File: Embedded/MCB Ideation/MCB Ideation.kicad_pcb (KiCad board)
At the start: 2 copper layers, 19.2 x 26.6 mm, 22 parts, among them J2 USB, J3 MicroSD, U1 ICM-20948, U2 BME280, U4 AP7366-33W5-7

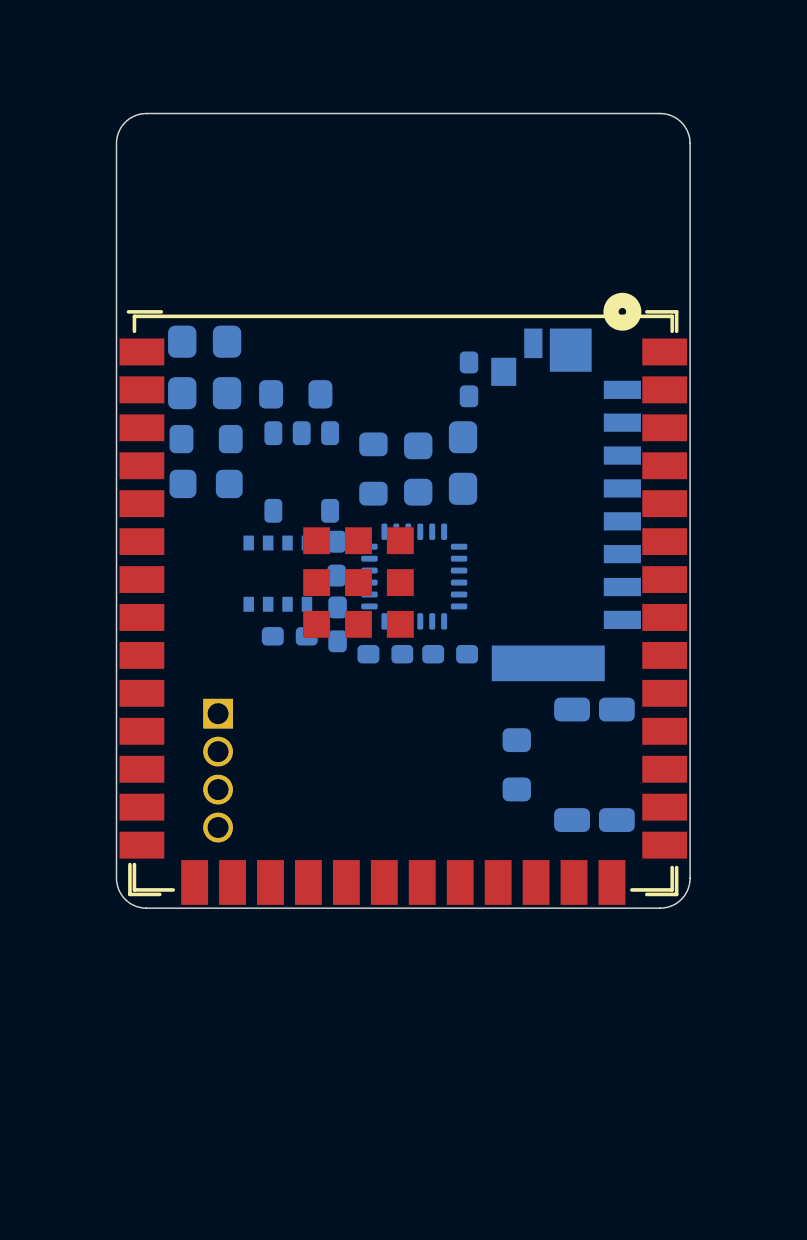
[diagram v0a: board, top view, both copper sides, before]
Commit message: Added Sensored
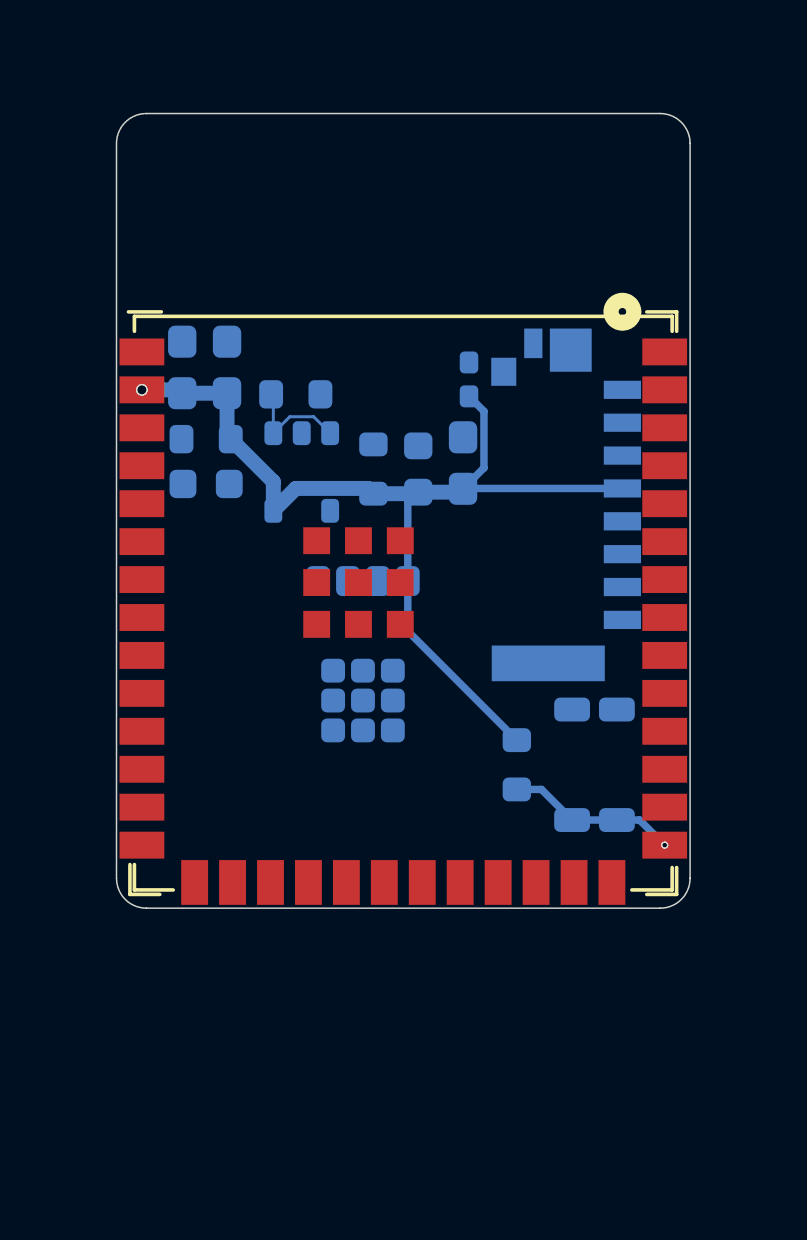
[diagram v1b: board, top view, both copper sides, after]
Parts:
- removed C1, C2, C3: 0.1uF, Capacitor_SMD:C_0402_1005Metric_Pad0.74x0.62mm_HandSolder
- removed C4, C5: 100nF, Capacitor_SMD:C_0402_1005Metric_Pad0.74x0.62mm_HandSolder
- removed J2: USB, Connector_PinSocket_1.27mm:PinSocket_1x04_P1.27mm_Vertical
- removed U2: BME280, Package_LGA:Bosch_LGA-8_2.5x2.5mm_P0.65mm_ClockwisePinNumbering
- U1: value ICM-20948 -> Sensored; footprint Sensor_Motion:InvenSense_QFN-24_3x3mm_P0.4mm -> Sensored:Sensored
- moved U1 4.49 mm to (138.7, 103.0), turned to 90 degrees
- turned C9 to 90 degrees
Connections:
- net /Vin renamed Net-(U4-EN)
- C12 pad 1: /3V3 -> +3V3
- C13 pad 1: /3V3 -> +3V3
- U1 pad 1: unconnected-(U1-NC-Pad1) -> +3V3
- U1 pad 2: unconnected-(U1-NC-Pad2) -> Sensor SDA
- U1 pad 3: unconnected-(U1-NC-Pad3) -> Sensor SCL
- U1 pad 4: unconnected-(U1-NC-Pad4) -> GND
- U4 pad 5: /3V3 -> +3V3
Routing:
- net +3V3: track 0.00 -> 33.2 mm, vias 0 -> 1
- net Net-(ESP1-GPIO0/BOOT): track 0.00 -> 5.72 mm, vias 0 -> 1
- net Net-(U4-EN): track 0.00 -> 3.69 mm

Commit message: Added Expansion Pins
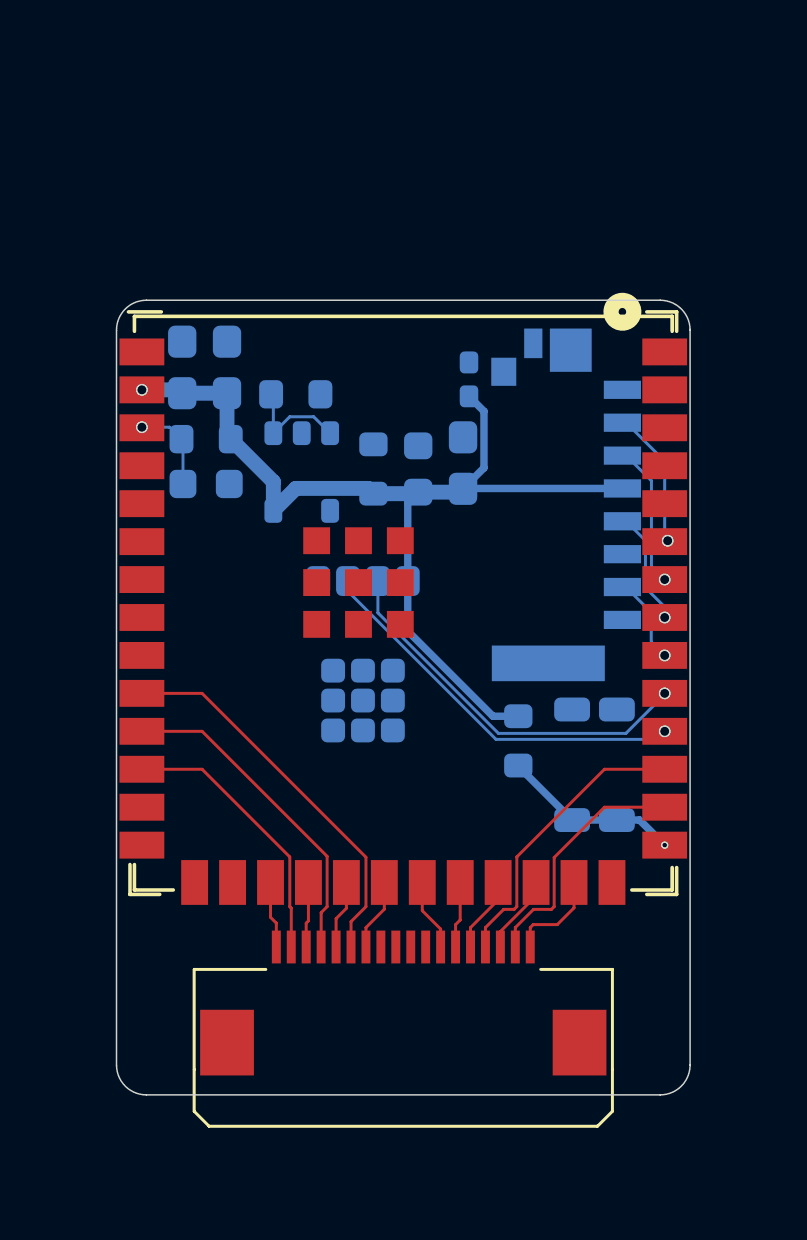
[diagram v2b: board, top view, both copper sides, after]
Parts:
- added U2: ~, FFC_Connector:FFC Aliexpress 0.5mm 18P, F.Cu at (140.0, 112.2)
- moved R2 0.80 mm to (143.8, 104.3)
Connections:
- ESP1 pad 10: unconnected-(ESP1-GPIO17/U1TXD/ADC2_CH6-Pad10) -> Exp 5
- ESP1 pad 11: unconnected-(ESP1-GPIO18/U1RXD/ADC2_CH7/CLK_OUT3-Pad11) -> Exp 3
- ESP1 pad 12: unconnected-(ESP1-GPIO8/TOUCH8/ADC1_CH7/SUBSPICS1-Pad12) -> Exp 1
- ESP1 pad 17: unconnected-(ESP1-GPIO9/TOUCH9/ADC1_CH8/FSPIHD/SUBSPIHD-Pad17) -> Exp 0
- ESP1 pad 18: unconnected-(ESP1-GPIO10/TOUCH10/ADC1_CH9/FSPICS0/FSPIIO4/SUBSPICS0-Pad18) -> Exp 2
- ESP1 pad 19: unconnected-(ESP1-GPIO11/TOUCH11/ADC2_CH0/FSPID/FSPIIO5/SUBSPID-Pad19) -> Exp 4
- ESP1 pad 20: unconnected-(ESP1-GPIO12/TOUCH12/ADC2_CH1/FSPICLK/FSPIIO6/SUBSPICLK-Pad20) -> Exp 6
- ESP1 pad 21: unconnected-(ESP1-GPIO13/TOUCH13/ADC2_CH2/FSPIQ/FSPIIO7/SUBSPIQ-Pad21) -> Exp 7
- ESP1 pad 22: unconnected-(ESP1-GPIO14/TOUCH14/ADC2_CH3/FSPIWP/FSPIDQS/SUBSPIWP-Pad22) -> Exp 8
- ESP1 pad 23: unconnected-(ESP1-GPIO21-Pad23) -> Exp 9
- ESP1 pad 24: unconnected-(ESP1-GPIO47/SPICLK_P/SUBSPICLK_P_DIFF-Pad24) -> Exp 11
- ESP1 pad 25: unconnected-(ESP1-GPIO48/SPICLK_N/SUBSPICLK_N_DIFF-Pad25) -> Exp 13
- ESP1 pad 28: unconnected-(ESP1-SPIIO6/GPIO35/FSPID/SUBSPID-Pad28) -> Exp 12
- ESP1 pad 29: unconnected-(ESP1-SPIIO7/GPIO36/FSPICLK/SUBSPICLK-Pad29) -> Exp 10
- ESP1 pad 30: unconnected-(ESP1-SPIDQS/GPIO37/FSPIQ/SUBSPIQ-Pad30) -> Sensor SCL
- ESP1 pad 31: unconnected-(ESP1-GPIO38/FSPIWP/SUBSPIWP-Pad31) -> Sensor SDA
- ESP1 pad 32: unconnected-(ESP1-MTCK/GPIO39/CLK_OUT3/SUBSPICS1-Pad32) -> SD SPI MISO
- ESP1 pad 33: unconnected-(ESP1-MTDO/GPIO40/CLK_OUT2-Pad33) -> SD SPI CLK
- ESP1 pad 34: unconnected-(ESP1-MTDI/GPIO41/CLK_OUT1-Pad34) -> SD SPI MOSI
- ESP1 pad 35: unconnected-(ESP1-MTMS/GPIO42-Pad35) -> SD SPI CS
- J3 pad 2: unconnected-(J3-Pad2) -> SD SPI CS
- J3 pad 3: unconnected-(J3-Pad3) -> SD SPI MOSI
- J3 pad 5: unconnected-(J3-Pad5) -> SD SPI CLK
- J3 pad 6: unconnected-(J3-Pad6) -> GND
- J3 pad 7: unconnected-(J3-Pad7) -> SD SPI MISO
- J3 pad G1: unconnected-(J3-PadG1) -> GND
- J3 pad G2: unconnected-(J3-PadG2) -> GND
- J3 pad G3: unconnected-(J3-PadG3) -> GND
- J3 pad G4: unconnected-(J3-PadG4) -> GND
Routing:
- net Sensor SCL: track 0.00 -> 13.1 mm, vias 0 -> 1
- net Exp 5: track 0.00 -> 13.0 mm
- net Sensor SDA: track 0.00 -> 12.9 mm, vias 0 -> 1
- net Exp 3: track 0.00 -> 11.1 mm
- net Exp 10: track 0.00 -> 9.82 mm
- net Exp 1: track 0.00 -> 9.20 mm
- net Exp 12: track 0.00 -> 8.28 mm
- net SD SPI CS: track 0.00 -> 5.04 mm, vias 0 -> 1
- net SD SPI MOSI: track 0.00 -> 4.81 mm, vias 0 -> 1
- net SD SPI CLK: track 0.00 -> 3.88 mm, vias 0 -> 1
- net Exp 13: track 0.00 -> 3.24 mm
- net Net-(ESP1-EN): track 0.00 -> 3.03 mm, vias 0 -> 1
- net SD SPI MISO: track 0.00 -> 2.94 mm, vias 0 -> 1
- net Exp 11: track 0.00 -> 2.65 mm
- net Exp 9: track 0.00 -> 2.54 mm
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
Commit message: Added USB Connectivity & Verified Expansion Pins
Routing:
- net USB -: track 0.00 -> 14.9 mm, vias 0 -> 2
- net USB +: track 0.00 -> 12.2 mm
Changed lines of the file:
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@@
 		(net 5)
+	)
+	(segment
+		(start 131.1 109.422206)
+		(end 134.602794 112.925)
+		(width 0.2)
+		(layer "F.Cu")
+		(net 9)
+	)
+	(segment
+		(start 140.25 112.025001)
+		(end 140.25 111.2)
+		(width 0.2)
+		(layer "F.Cu")
+		(net 9)
+	)
+	(segment
+		(start 140.225 112.050001)
+		(end 140.25 112.025001)
+		(width 0.2)
+		(layer "F.Cu")
+		(net 9)
+	)
+	(segment
+		(start 140.225 112.2932)
+		(end 140.225 112.050001)
+		(width 0.2)
+		(layer "F.Cu")
+		(net 9)
+	)
+	(segment
+		(start 139.5932 112.925)
+		(end 140.225 112.2932)
+		(width 0.2)
+		(layer "F.Cu")
+		(net 9)
+	)
+	(segment
+		(start 134.602794 112.925)
+		(end 139.5932 112.925)
+		(width 0.2)
+		(layer "F.Cu")
+		(net 9)
+	)
+	(segment
+		(start 131.1 108.75)
+		(end 131.1 109.422206)
+		(width 0.2)
+		(layer "F.Cu")
+		(net 9)
+	)
+	(via
+		(at 131.1 108.75)
+		(size 0.4)
+		(drill 0.3)
+		(layers "F.Cu" "B.Cu")
+		(net 9)
+	)
+	(via
+		(at 131.25 106.52)
+		(size 0.4)
+		(drill 0.3)
+		(layers "F.Cu" "B.Cu")
+		(net 9)
+	)
+	(segment
+		(start 131.25 108.6)
+		(end 131.1 108.75)
+		(width 0.2)
+		(layer "B.Cu")
+		(net 9)
+	)
+	(segment
+		(start 131.25 106.52)
+		(end 131.25 108.6)
+		(width 0.2)
+		(layer "B.Cu")
+		(net 9)
+	)
+	(segment
+		(start 139.775 112.1068)
+		(end 139.775 112.050001)
+		(width 0.2)
+		(layer "F.Cu")
+		(net 10)
+	)
+	(segment
+		(start 131.6 108.14)
+		(end 131.6 109.25)
+		(width 0.2)
+		(layer "F.Cu")
+		(net 10)
+	)
+	(segment
+		(start 139.75 112.025001)
+		(end 139.75 111.2)
+		(width 0.2)
+		(layer "F.Cu")
+		(net 10)
+	)
+	(segment
+		(start 139.775 112.050001)
+		(end 139.75 112.025001)
+		(width 0.2)
+		(layer "F.Cu")
+		(net 10)
+	)
+	(segment
+		(start 131.25 107.79)
+		(end 131.6 108.14)
+		(width 0.2)
+		(layer "F.Cu")
+		(net 10)
+	)
+	(segment
+		(start 139.4068 112.475)
+		(end 139.775 112.1068)
+		(width 0.2)
+		(layer "F.Cu")
+		(net 10)
+	)
+	(segment
+		(start 131.6 109.25)
+		(end 134.825 112.475)
+		(width 0.2)
+		(layer "F.Cu")
+		(net 10)
+	)
+	(segment
+		(start 134.825 112.475)
+		(end 139.4068 112.475)
+		(width 0.2)
+		(layer "F.Cu")
+		(net 10)
 	)
 	(via

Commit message: Added Secondary Expansion (Comms Link)
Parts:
- added U3: ~, FFC_Connector:FFC Aliexpress 0.5mm 6P, B.Cu at (140.0, 112.2)
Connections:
- net Net-(U4-EN) renamed +5V
- ESP1 pad 8: unconnected-(ESP1-GPIO15/U0RTS/ADC2_CH4/XTAL_32K_P-Pad8) -> EXP UART TX
- ESP1 pad 9: unconnected-(ESP1-GPIO16/U0CTS/ADC2_CH5/XTAL_32K_N-Pad9) -> EXP UART RX
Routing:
- net EXP UART TX: track 0.00 -> 15.5 mm, vias 0 -> 1
- net EXP UART RX: track 0.00 -> 13.9 mm, vias 0 -> 1

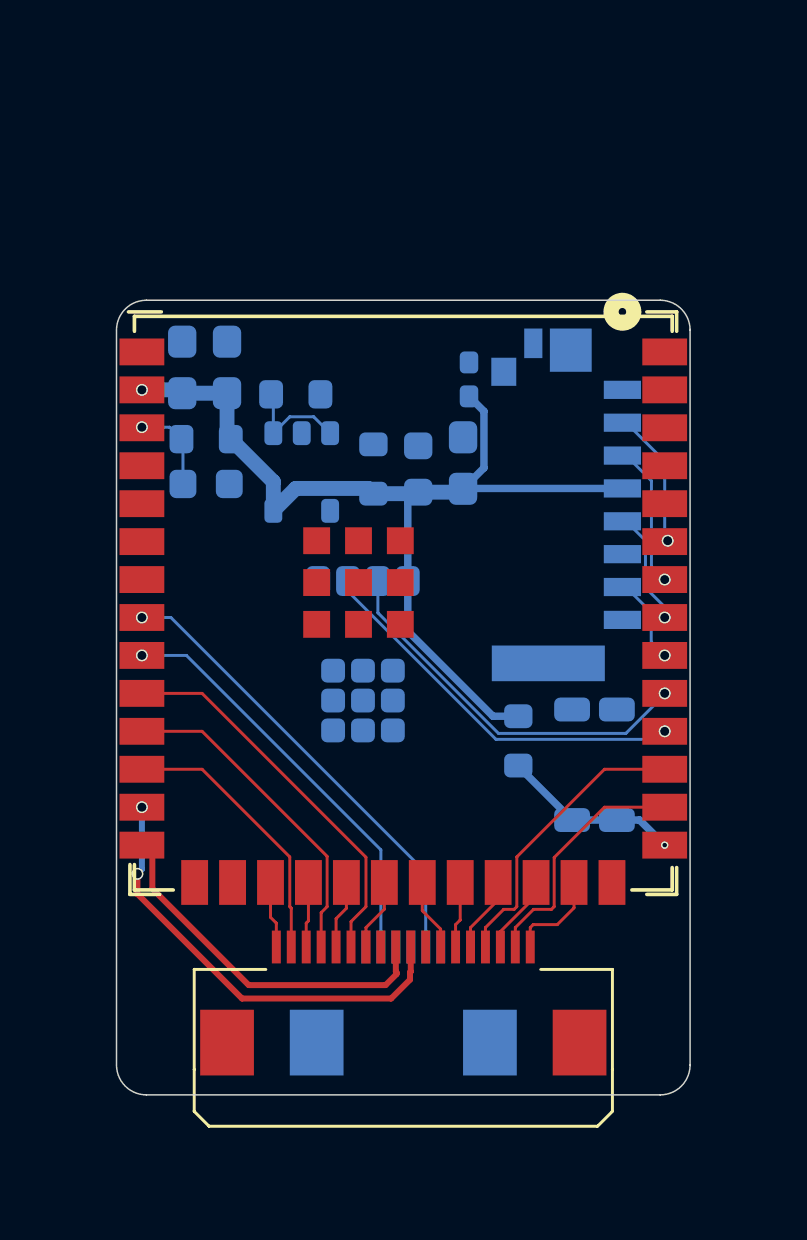
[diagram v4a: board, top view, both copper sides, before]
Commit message: Added USB and Power Ports
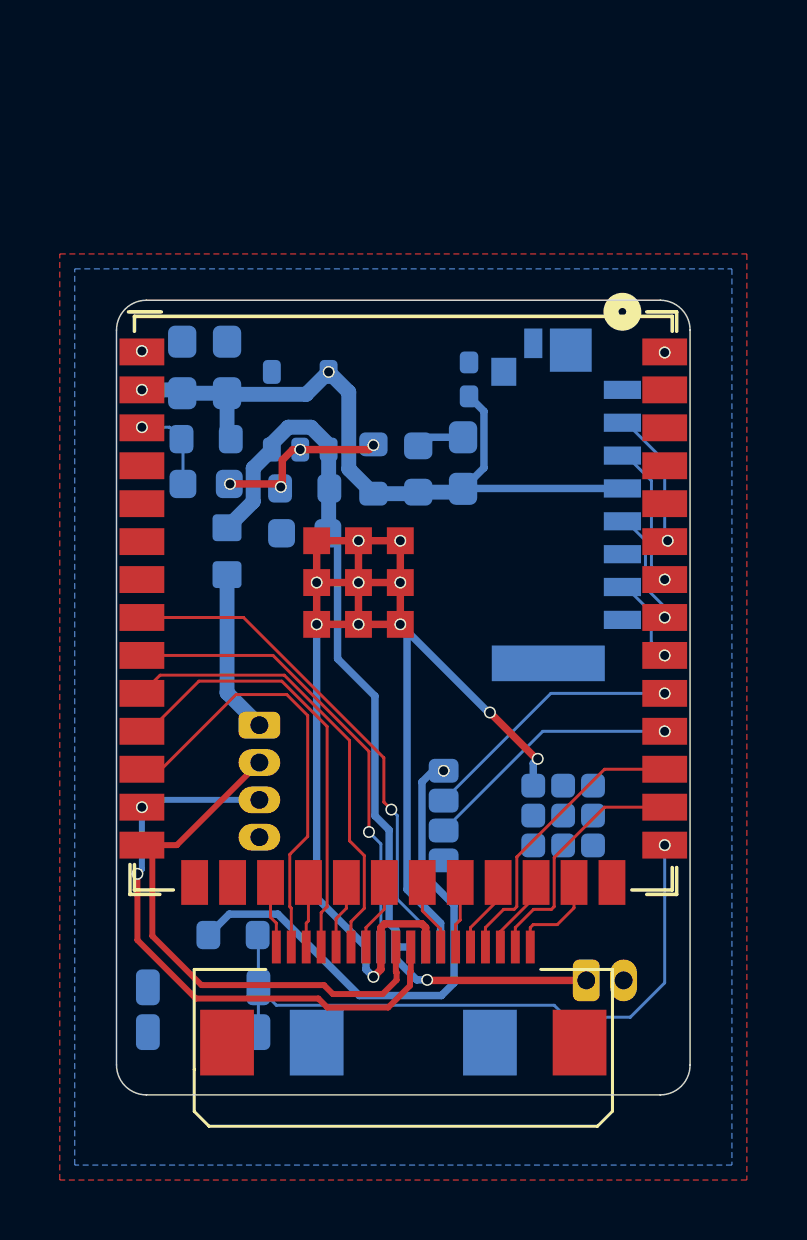
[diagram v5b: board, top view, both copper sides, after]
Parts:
- added C1: 10uF, Capacitor_SMD:C_0603_1608Metric, B.Cu at (136.7, 97.3)
- added J1: USB, Connector_Hirose:Hirose_DF13-04P-1.25DS_1x04_P1.25mm_Horizontal, B.Cu at (135.2, 103.8)
- added J2: Power, Connector_Hirose:Hirose_DF13-02P-1.25DS_1x02_P1.25mm_Horizontal, B.Cu at (146.1, 112.3)
- added L1: MPZ1608S601ATA00, Ferrite_Bead_MPZ1608S601ATA00:INDC1608X95N, B.Cu at (134.1, 98.0)
- U2: value ~ -> Expansion
- U3: value ~ -> Comms Link Expansion
- moved BootSW1 15.5 mm to (133.3, 113.3), turned to 180 degrees
- moved R2 11.6 mm to (134.3, 110.8), turned to 0 degrees
- moved U1 7.73 mm to (145.3, 106.8), turned to 180 degrees
- moved C11 3.16 mm to (136.7, 95.8), turned to 180 degrees
- moved U4 2.05 mm to (136.6, 93.2), turned to 0 degrees
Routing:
- net GND: track 0.00 -> 59.9 mm, vias 0 -> 17
- net +5V: track 3.69 -> 31.3 mm, vias 0 -> 1
- net Net-(ESP1-GPIO0/BOOT): track 6.02 -> 22.4 mm
- net +3V3: track 32.9 -> 42.8 mm, vias 1 -> 3
- net USB +: track 12.2 -> 18.6 mm
- net Exp 1: track 9.20 -> 14.9 mm
- net Net-(J1-Pin_1): track 0.00 -> 5.49 mm
- net USB -: track 14.9 -> 20.2 mm
- net Sensor SCL: track 13.1 -> 8.78 mm
- net Sensor SDA: track 12.9 -> 8.93 mm
- net Exp 3: track 11.1 -> 15.0 mm
- net Exp 5: track 13.0 -> 15.4 mm
- net EXP UART RX: track 13.9 -> 15.6 mm
- net EXP UART TX: track 15.5 -> 17.0 mm
- added copper zone on F.Cu, net +3V3
- added copper zone on B.Cu, net GND

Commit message: Rerouted Some Components
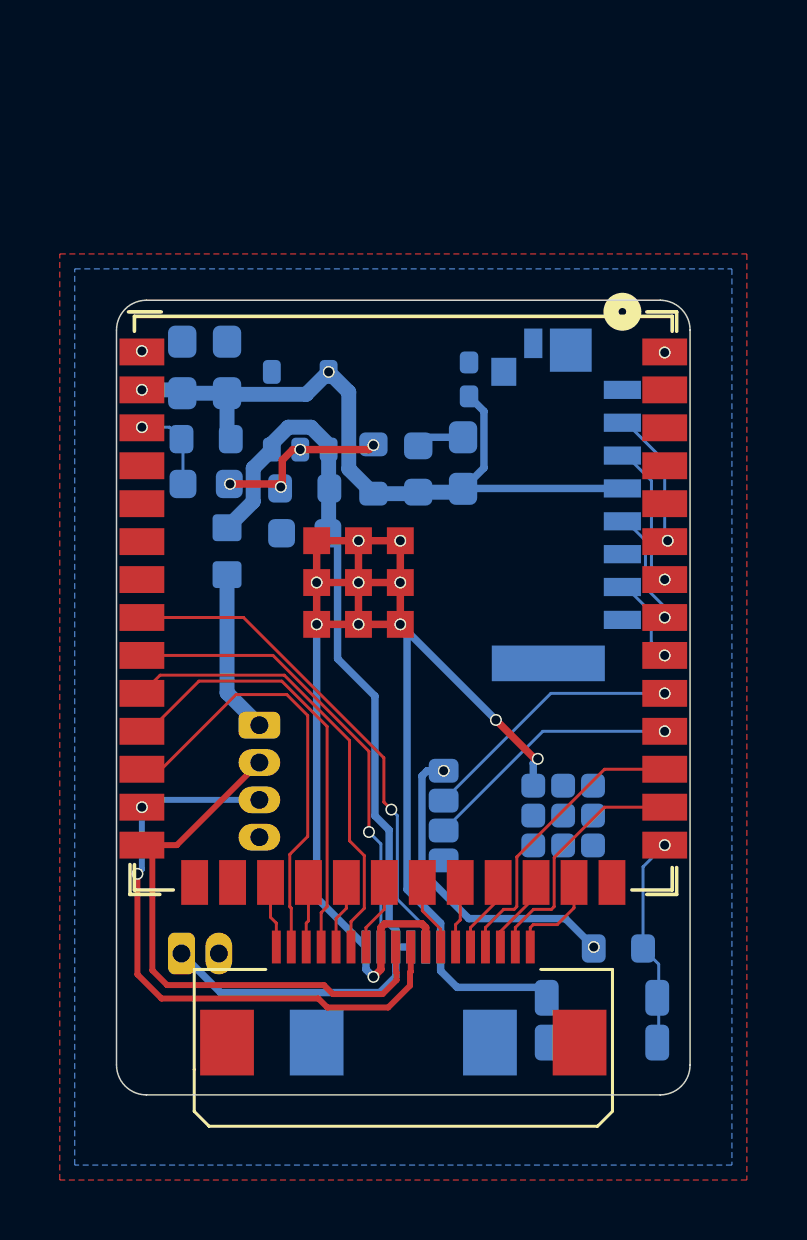
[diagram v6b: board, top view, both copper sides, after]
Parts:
- moved J2 13.6 mm to (132.6, 111.4)
- moved BootSW1 13.4 mm to (146.7, 113.7)
- moved R2 12.9 mm to (147.2, 111.2)
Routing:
- net Net-(ESP1-GPIO0/BOOT): track 22.4 -> 6.78 mm
- net +3V3: track 42.8 -> 35.7 mm, vias 3 -> 4
- net GND: track 59.9 -> 64.5 mm
- net +5V: track 31.3 -> 33.1 mm, vias 1 -> 0
- net USB -: track 20.2 -> 20.9 mm
- net USB +: track 18.6 -> 19.2 mm
